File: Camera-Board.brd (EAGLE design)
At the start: 123.2 x 64.8 mm, 87 parts, among them J1 RJ45KEYSTONE-942, J10 BNC, J11 BNC, J12 BNC, J13 BNC, J14 BNC, J2 JTAG_ARM_10PIN, J3 APP_2POS_CONFIG12V_HORIZ, J4 BNC, J5 BNC, J6 BNC, J7 BNC, J9 BNC, U1 TM4C1294NCPDT, U2 HX1198FNL, U3 SLVU2.8-4, U4 OKI-78SR-5/1.5-W36HC, U5 TPS73733DCQ, U6 MAX4312ESE, U8 MAX4312ESE, Y1 NX3225GA, Y2 CRYATL_32K_SMD

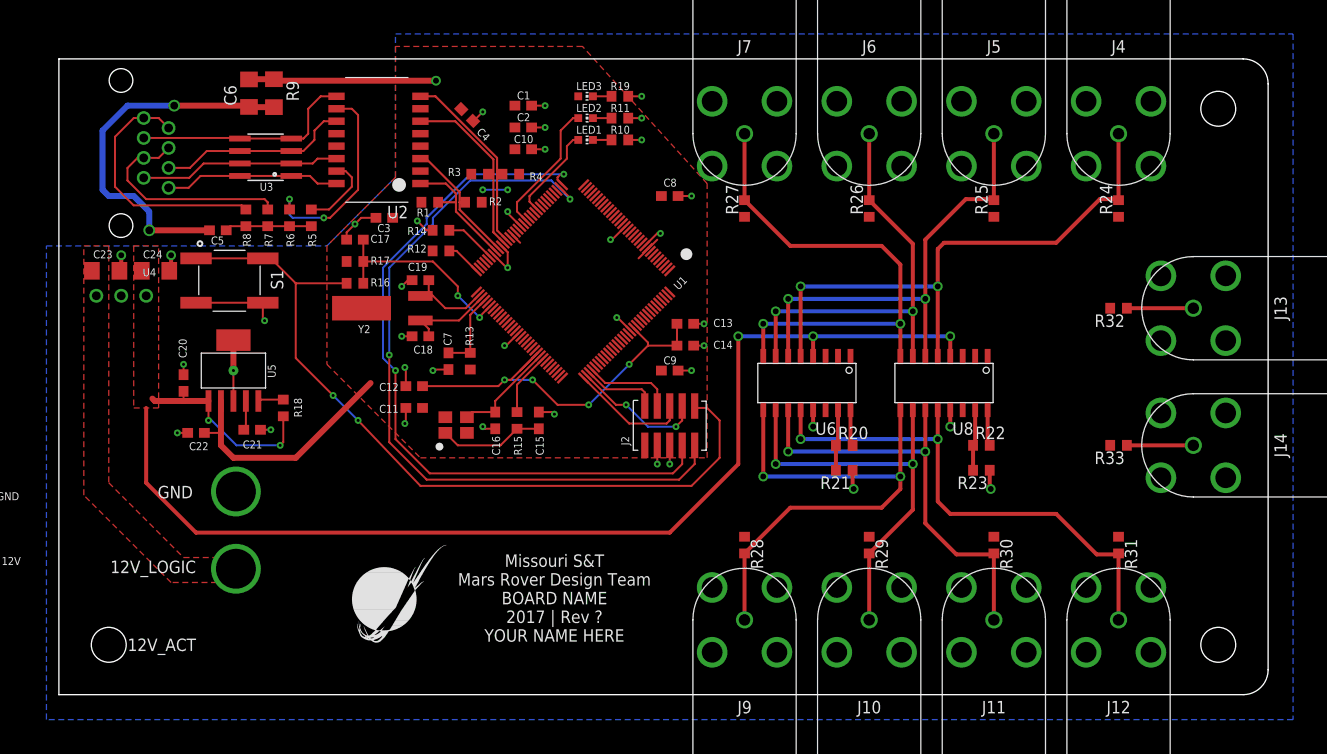
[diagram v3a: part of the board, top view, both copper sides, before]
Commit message: Finished routing board
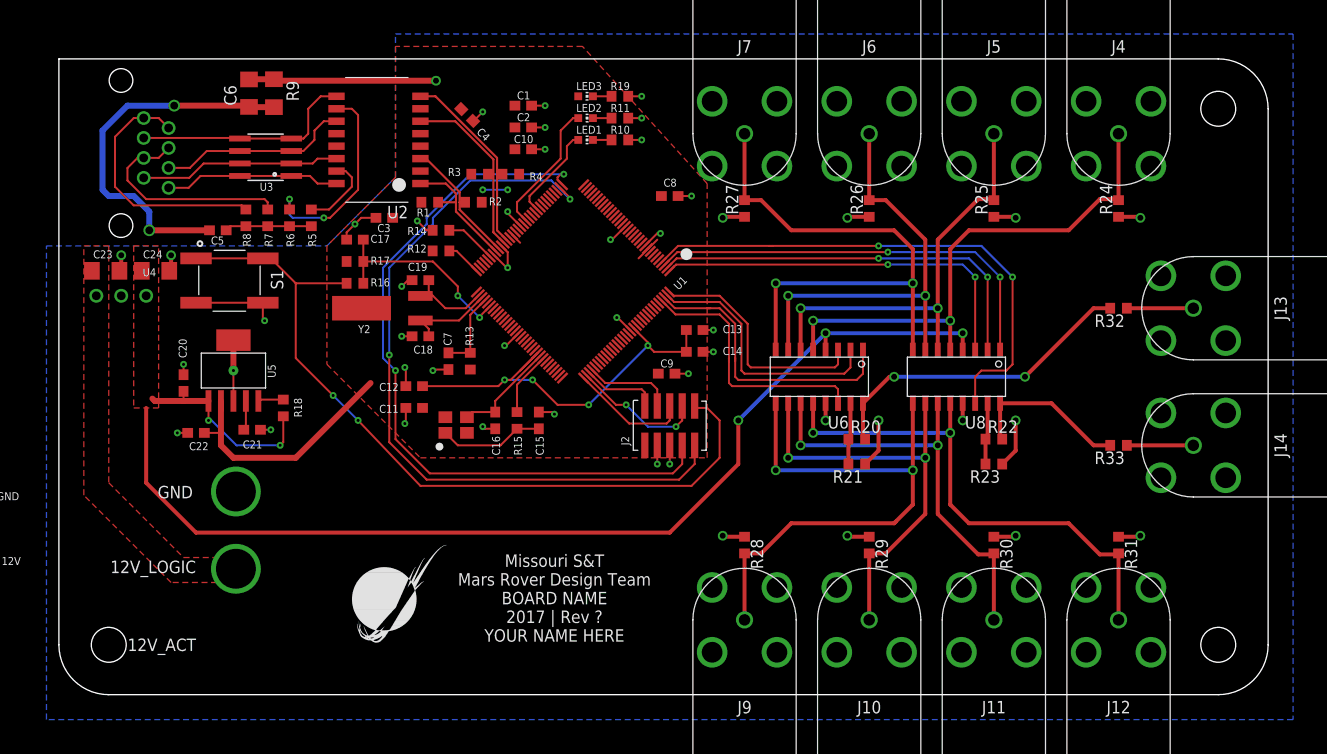
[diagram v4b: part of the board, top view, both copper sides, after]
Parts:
- moved R20 1.42 mm to (81.3, 26.0)
- moved R21 1.42 mm to (81.3, 23.5)
- moved R22 1.42 mm to (95.2, 26.0)
- moved R23 1.42 mm to (95.2, 23.5)
- moved U6 1.42 mm to (77.5, 32.4)
- moved U8 1.42 mm to (91.4, 32.4)
- moved C14 1.14 mm to (64.8, 34.9)
- moved C13 1.14 mm to (64.8, 37.1)
- moved C9 0.45 mm to (61.9, 32.7)
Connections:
- net MUX0_0: now also U1.P$128
- net MUX0_1: now also U1.P$127
- net MUX0_2: now also U1.P$126
- net MUX0_SHDN: now also U1.P$125
- net MUX1_0: now also U1.P$1
- net MUX1_1: now also U1.P$2
- net MUX1_2: now also U1.P$3
- net MUX1_SHDN: now also U1.P$4
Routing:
- net MUX1_SHDN: track 0.00 -> 53.7 mm, vias 0 -> 2
- net MUX1_2: track 0.00 -> 43.3 mm, vias 0 -> 2
- net MUX1_1: track 0.00 -> 41.3 mm, vias 0 -> 2
- net MUX1_0: track 0.00 -> 39.4 mm, vias 0 -> 2
- net MUX0_2: track 0.00 -> 30.2 mm
- net CAM_OUT0: track 3.74 -> 32.9 mm, vias 0 -> 2
- net MUX0_SHDN: track 0.00 -> 27.0 mm
- net MUX0_1: track 0.00 -> 26.8 mm
- net GND: track 98.0 -> 122.7 mm, vias 40 -> 48
- net MUX0_0: track 0.00 -> 24.3 mm
- net CAM_OUT1: track 3.74 -> 16.7 mm
- net CAM_IN0: track 59.4 -> 53.4 mm
- net CAM_IN3: track 52.0 -> 57.1 mm
- net +5V_LOGIC: track 131.9 -> 127.6 mm
- net CAM_IN1: track 47.3 -> 43.8 mm
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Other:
- outline, holes or cut-outs redrawn

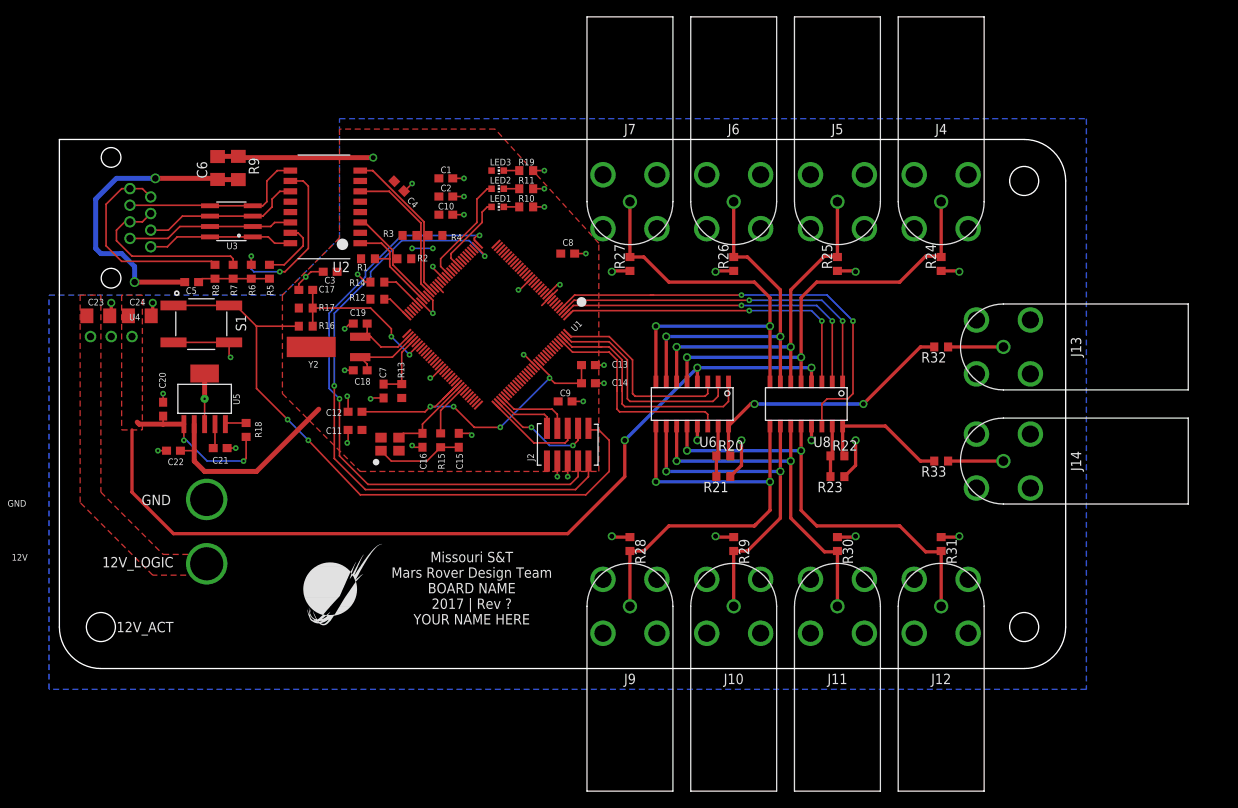
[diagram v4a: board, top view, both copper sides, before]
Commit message: Final touches
Made board larger
Added more space between BNCs
Added more mounting holes
Updated Slik text and added signature
Arranged component labels
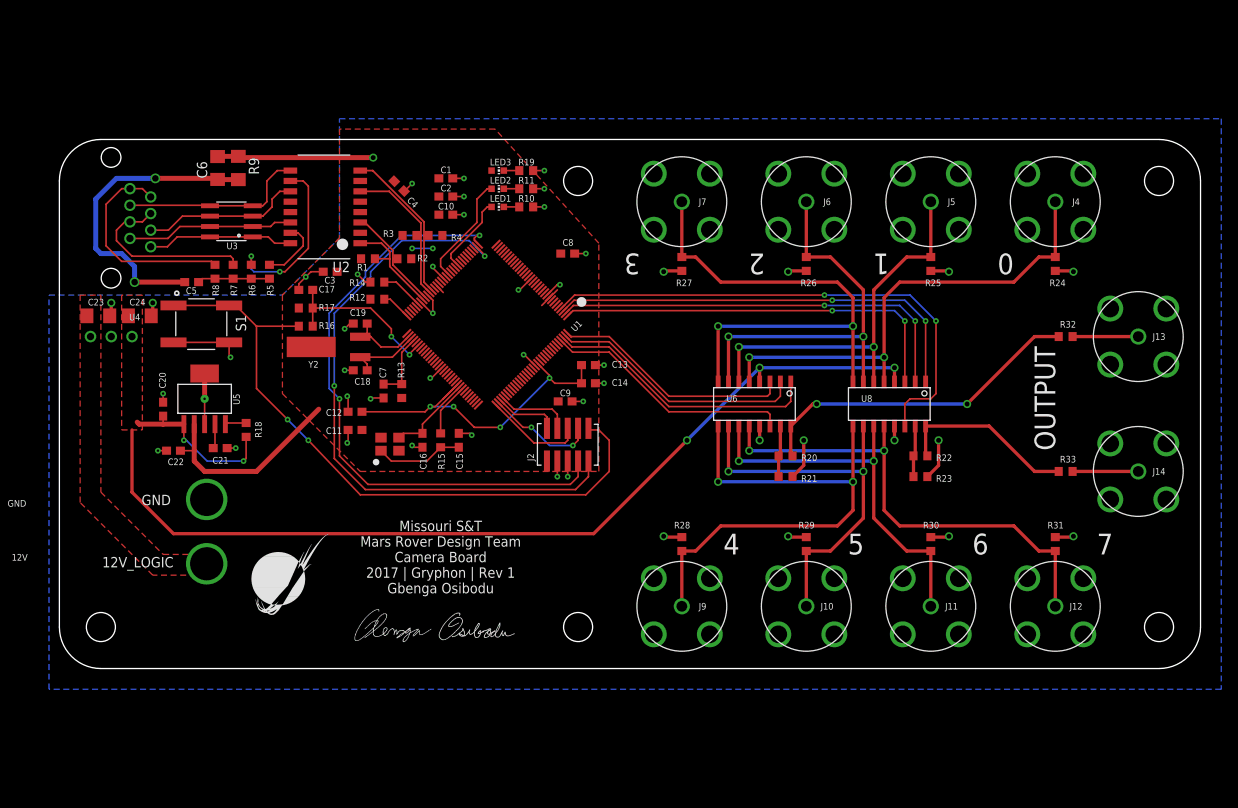
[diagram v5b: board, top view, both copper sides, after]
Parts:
- added U$6, U$7: MOUNTING_HOLE#6, MRDT-Hardware:#6_SCREW
- added U$8: SIG3, sig:SIG3
- J10, J11, J12, J13, J14, J4, J5, J6, J7, J9: value BNC -> BNCVERT; device MRDT-Connectors:MOLEX-0731711640-BNC -> MRDT-Connectors:MOLEX-0731711900-BNC
- moved J13 16.6 mm to (132.1, 40.6)
- moved J14 16.6 mm to (132.1, 24.1)
- moved U$2 16.5 mm to (134.6, 5.08)
- moved U$4 16.5 mm to (134.6, 59.7)
- moved R32 15.3 mm to (123.2, 40.6)
- moved R33 15.3 mm to (123.2, 24.1)
- moved J12 14.0 mm to (121.9, 7.62)
- moved J4 14.0 mm to (121.9, 57.1)
- moved R24 14.0 mm to (121.9, 49.5)
- moved R31 14.0 mm to (121.9, 15.2)
- moved J11 11.4 mm to (106.7, 7.62)
- moved J5 11.4 mm to (106.7, 57.1)
- moved R25 11.4 mm to (106.7, 49.5)
- moved R30 11.4 mm to (106.7, 15.2)
- moved R22 10.2 mm to (105.4, 26.0)
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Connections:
- net CAM_OUT0: now also R22.2, R33.2, U8.16; no longer R20.2, R32.2, U6.16
- net CAM_OUT1: now also R20.2, R32.2, U6.16; no longer R22.2, R33.2, U8.16
- net MUX0_0: now also U1.P$1, U8.3; no longer U1.P$128, U6.3
- net MUX0_1: now also U1.P$2, U8.2; no longer U1.P$127, U6.2
- net MUX0_2: now also U1.P$3, U8.1; no longer U1.P$126, U6.1
- net MUX0_SHDN: now also U1.P$4, U8.14; no longer U1.P$125, U6.14
- net MUX1_0: now also U1.P$128, U6.3; no longer U1.P$1, U8.3
- net MUX1_1: now also U1.P$127, U6.2; no longer U1.P$2, U8.2
- net MUX1_2: now also U1.P$126, U6.1; no longer U1.P$3, U8.1
- net MUX1_SHDN: now also U1.P$125, U6.14; no longer U1.P$4, U8.14
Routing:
- net MUX0_SHDN: track 27.0 -> 63.9 mm, vias 0 -> 2
- net MUX0_0: track 24.3 -> 49.5 mm, vias 0 -> 2
- net MUX0_1: track 26.8 -> 51.5 mm, vias 0 -> 2
- net CAM_OUT1: track 16.7 -> 41.1 mm, vias 0 -> 2
- net MUX0_2: track 30.2 -> 53.4 mm, vias 0 -> 2
- net MUX1_SHDN: track 53.7 -> 30.8 mm, vias 2 -> 0
- net CAM_OUT0: track 32.9 -> 22.3 mm, vias 2 -> 0
- net MUX1_0: track 39.4 -> 29.5 mm, vias 2 -> 0
- net MUX1_1: track 41.3 -> 31.7 mm, vias 2 -> 0
- net MUX1_2: track 43.3 -> 34.0 mm, vias 2 -> 0
- net +5V_LOGIC: track 127.6 -> 135.2 mm
- net CAM_IN0: track 53.4 -> 59.8 mm
- net CAM_IN3: track 57.1 -> 63.4 mm
- net CAM_IN7: track 53.4 -> 59.6 mm
- net CAM_IN4: track 57.3 -> 63.4 mm
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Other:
- board size 123.2 x 64.8 mm -> 139.7 x 64.8 mm
- board text added: "0"
- board text added: "1"
- board text added: "2"
- board text added: "3"
- board text added: "4"
- board text added: "5"
- board text added: "6"
- board text added: "7"
- board text added: "Missouri S&T Mars Rover Design Team Camera Board 2017 | Gryphon | Rev 1 Gbenga Osibodu"
- board text added: "OUTPUT"
- board text removed: "12V_ACT"
- board text removed: "Missouri S&T Mars Rover Design Team BOARD NAME 2017 | Rev ? YOUR NAME HERE"
